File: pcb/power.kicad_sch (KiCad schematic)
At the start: 22 parts, among them U1 LDLN025M25R, U13 TS3312AQPR, U2 LM27762DSST

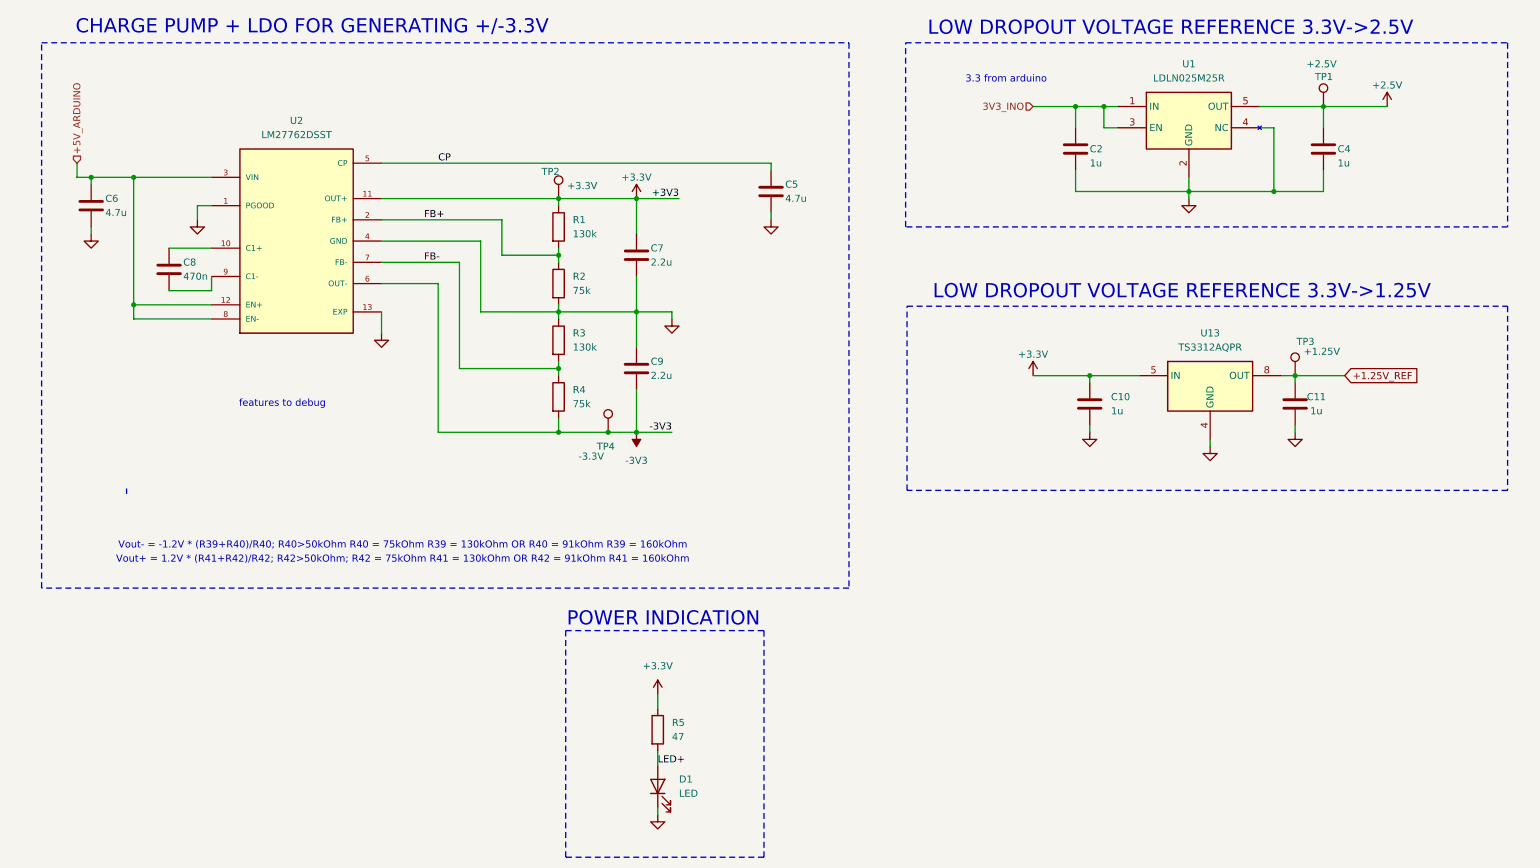
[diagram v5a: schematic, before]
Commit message: feat: Improve PCB design after tests of rev 0.8
- Added new generation of humidity sensor
- New silkscreen information for different components
- Added additional testpoints
- Removed PWM path for ultrasound transmitter
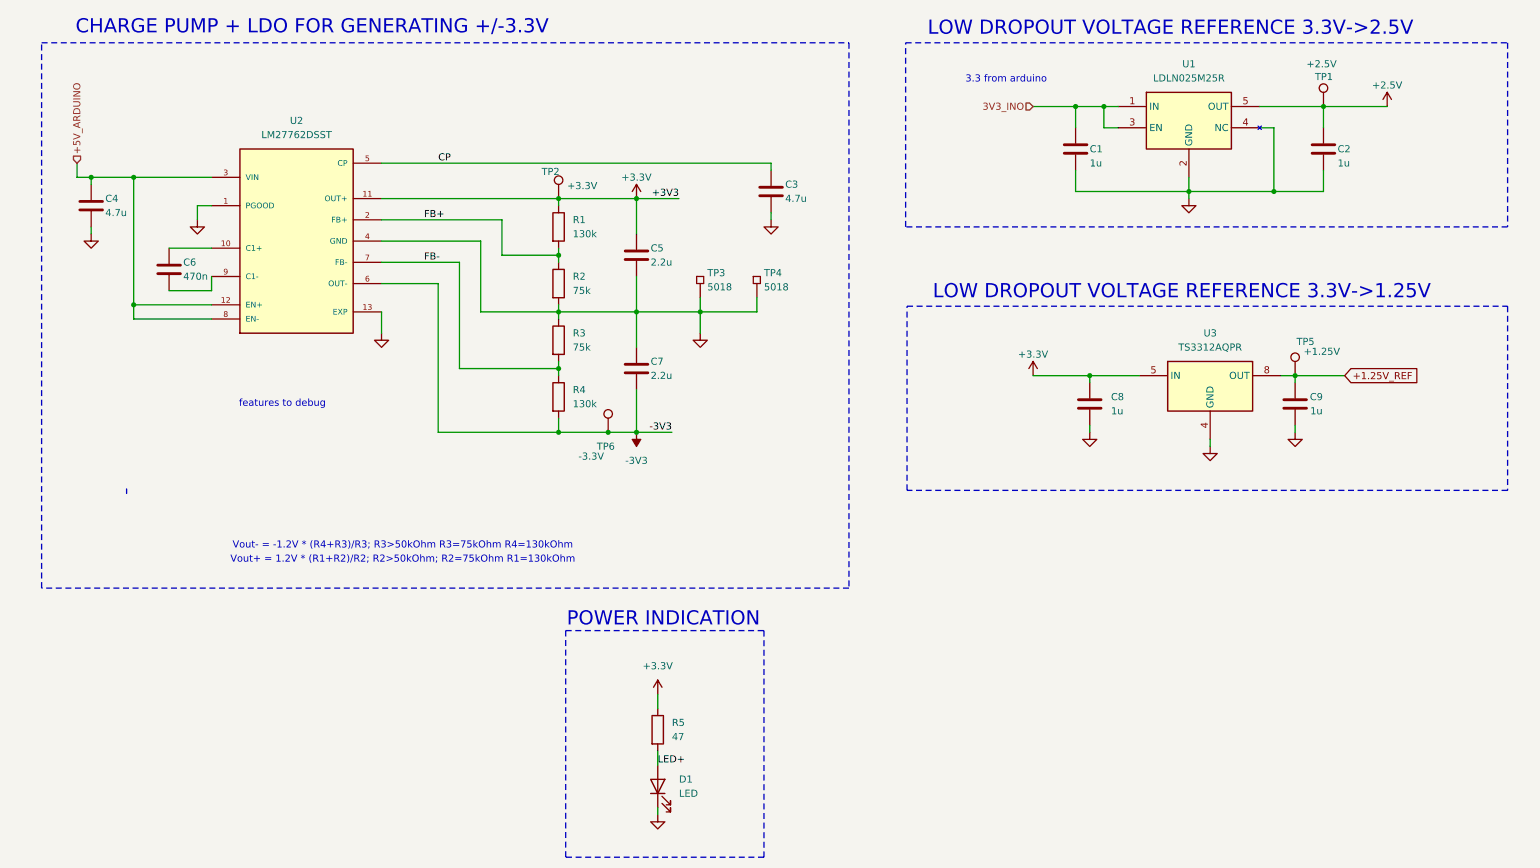
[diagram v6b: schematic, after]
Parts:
- added TP3, TP4: 5018, SensEdu:5018, symbol SensEdu:5018
- C1: renamed from C2; footprint Capacitor_SMD:C_0603_1608Metric -> SensEdu:C_0603_1608Metric
- C2: renamed from C4; footprint Capacitor_SMD:C_0603_1608Metric -> SensEdu:C_0603_1608Metric
- C3: renamed from C5; footprint Capacitor_SMD:C_0805_2012Metric -> SensEdu:C_0805_2012Metric
- C4: renamed from C6; footprint Capacitor_SMD:C_0805_2012Metric -> SensEdu:C_0805_2012Metric
- C5: renamed from C7; footprint Capacitor_SMD:C_0805_2012Metric -> SensEdu:C_0805_2012Metric
- C6: renamed from C8; footprint Capacitor_SMD:C_0603_1608Metric -> SensEdu:C_0603_1608Metric
- C7: renamed from C9; footprint Capacitor_SMD:C_0805_2012Metric -> SensEdu:C_0805_2012Metric
- C8: renamed from C10; footprint Capacitor_SMD:C_0603_1608Metric -> SensEdu:C_0603_1608Metric
- C9: renamed from C11; footprint Capacitor_SMD:C_0603_1608Metric -> SensEdu:C_0603_1608Metric
- D1: footprint LED_SMD:LED_0805_2012Metric -> SensEdu:LED_0805_2012Metric
- R1, R2, R5: footprint Resistor_SMD:R_0603_1608Metric -> SensEdu:R_0603_1608Metric
- R3: value 130k -> 75k; footprint Resistor_SMD:R_0603_1608Metric -> SensEdu:R_0603_1608Metric
- R4: value 75k -> 130k; footprint Resistor_SMD:R_0603_1608Metric -> SensEdu:R_0603_1608Metric
- TP1, TP2: footprint TestPoint:TestPoint_THTPad_D2.0mm_Drill1.0mm -> SensEdu:TestPoint_THTPad_D2.0mm_Drill1.0mm
- TP5: renamed from TP3; footprint TestPoint:TestPoint_THTPad_D2.0mm_Drill1.0mm -> SensEdu:TestPoint_THTPad_D2.0mm_Drill1.0mm
- TP6: renamed from TP4; footprint TestPoint:TestPoint_THTPad_D2.0mm_Drill1.0mm -> SensEdu:TestPoint_THTPad_D2.0mm_Drill1.0mm
- U1: footprint SamacSys_Parts:SOT95P280X145-5N -> SensEdu:SOT95P280X145-5N
- U3: renamed from U13; footprint SamacSys_Parts:TS3312AQPR -> SensEdu:TS3312AQPR
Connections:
- net GND: now also TP3.1, TP4.1
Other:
- note added: "Vout+ = 1.2V * (R1+R2)/R2; R2>50kOhm; R2=75kOhm R1=130kOhm"
- note added: "Vout- = -1.2V * (R4+R3)/R3; R3>50kOhm R3=75kOhm R4=130kOhm"
- note removed: "Vout+ = 1.2V * (R41+R42)/R42; R42>50kOhm; R42 = 75kOhm R41 = 130kOhm OR R42 = 91kOhm R41 = 160kOhm"
- note removed: "Vout- = -1.2V * (R39+R40)/R40; R40>50kOhm R40 = 75kOhm R39 = 130kOhm OR R40 = 91kOhm R39 = 160kOhm"

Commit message: refactor: Remove unnecessary comments
- Regenerate schematics
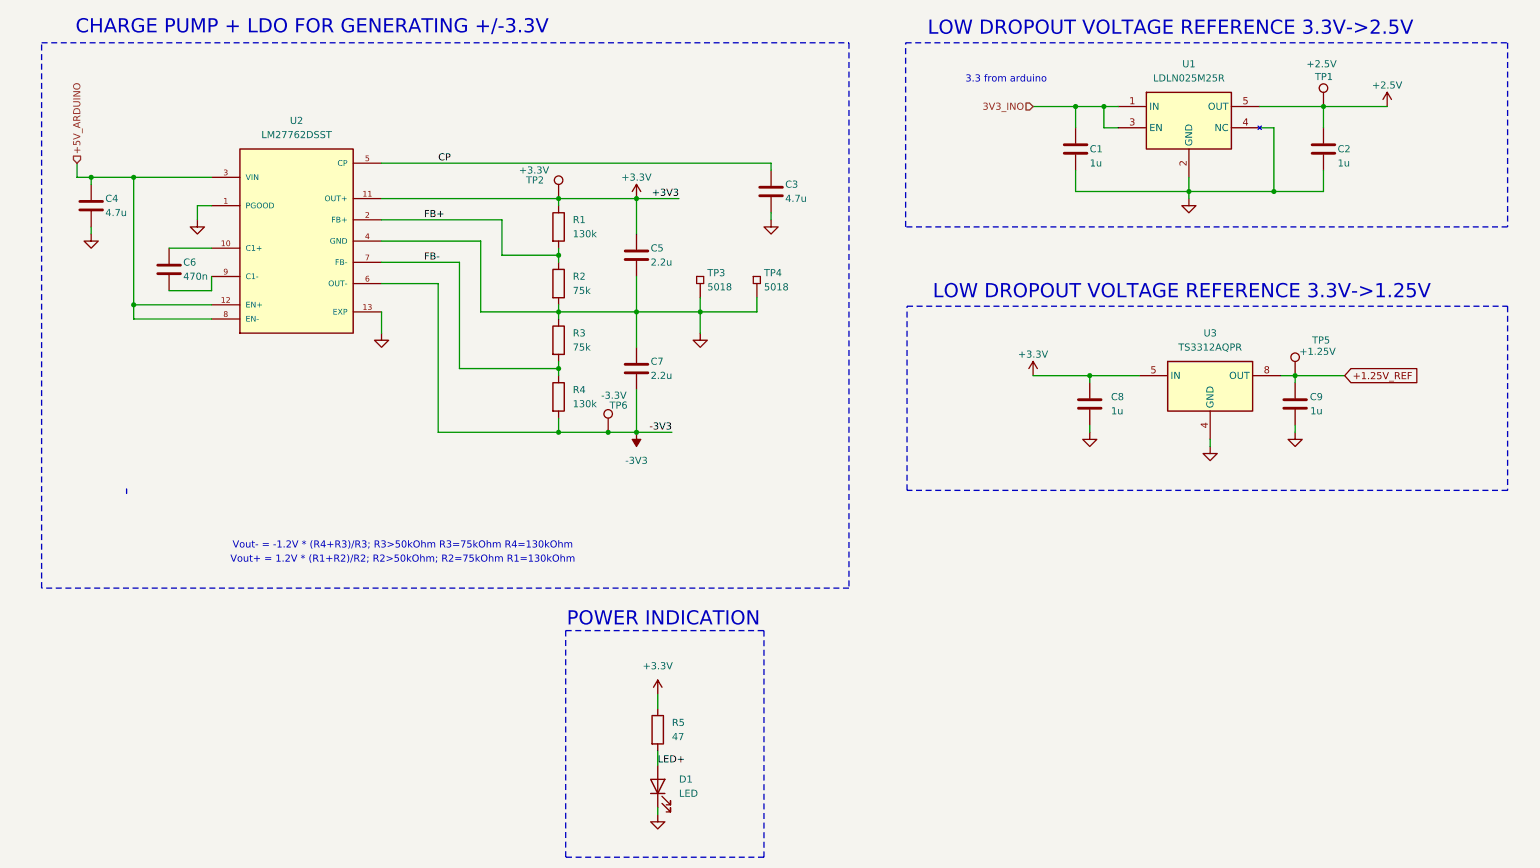
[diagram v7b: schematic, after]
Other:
- note removed: "features to debug"
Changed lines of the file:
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@@
-		)
-	)
-	(text "features to debug"
-		(exclude_from_sim no)
-		(at 59.69 87.63 0)
-		(effects
-			(font
-				(size 1.27 1.27)
-			)
 		)
 	)
@@
 		(dnp no)
 		(property "Reference" "TP5"
-			(at 241.554 76.454 0)
+			(at 244.348 76.2 0)
 			(effects
 				(font
@@
 		)
 		(property "Value" "+1.25V"
-			(at 242.824 78.232 0)
+			(at 242.062 78.232 0)
 			(effects
 				(font
@@
 		(dnp no)
 		(property "Reference" "TP6"
-			(at 116.078 95.25 0)
+			(at 118.364 87.884 0)
 			(effects
 				(font
@@
 		)
 		(property "Value" "-3.3V"
-			(at 112.776 97.028 0)
+			(at 116.84 86.106 0)
 			(effects
 				(font
@@
 		(dnp no)
 		(property "Reference" "TP2"
-			(at 106.172 45.974 0)
+			(at 103.378 47.498 0)
 			(effects
 				(font
@@
 		)
 		(property "Value" "+3.3V"
-			(at 110.744 48.514 0)
-			(effects
-				(font
+			(at 102.108 45.72 0)
+			(effects
+				(font
